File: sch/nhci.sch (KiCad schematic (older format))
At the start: 17 parts, among them IC1 74LVC8T245RHLRG4, IC2 74LVC8T245RHLRG4, IC3 74LVC8T245RHLRG4, IC4 74LVC8T245RHLRG4, IC5 74LVC8T245RHLRG4, SW1 SW_Push_Open, U1 PCMCIA_BOARD

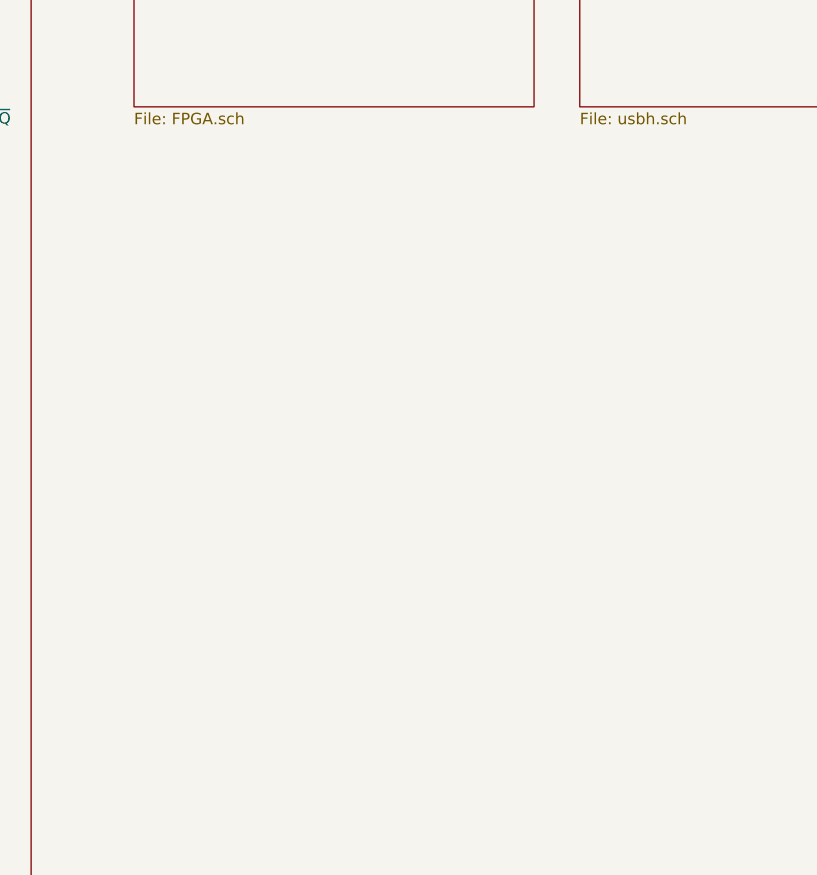
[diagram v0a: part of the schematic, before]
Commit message: Add pullup resistors
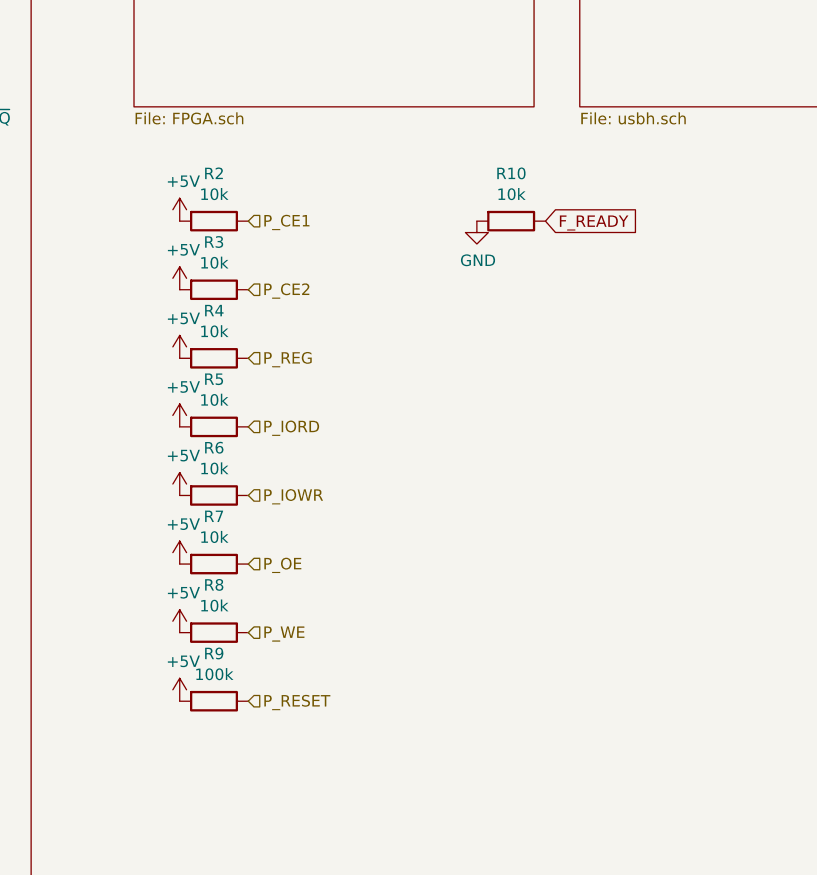
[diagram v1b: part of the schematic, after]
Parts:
- added R10, R2, R3, R4, R5, R6, R7, R8: 10k, Resistor_SMD:R_0402_1005Metric, symbol Device:R
- added R9: 100k, Resistor_SMD:R_0402_1005Metric, symbol Device:R
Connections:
- net +5V: now also R2.2, R3.2, R4.2, R5.2, R6.2, R7.2, R8.2, R9.2
- net F_READY: now also R10.1
- net GND: now also R10.2
- net P_CE1: now also R2.1
- net P_CE2: now also R3.1
- net P_IORD: now also R5.1
- net P_IOWR: now also R6.1
- net P_OE: now also R7.1
- net P_REG: now also R4.1
- net P_RESET: now also R9.1
- net P_WE: now also R8.1
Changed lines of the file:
@@
 F1 "usbh.sch" 50
 $EndSheet
+$Comp
+L Device:R R2
+U 1 1 60E72B90
+P 7550 4300
+F 0 "R2" V 7343 4300 50  0000 C CNN
+F 1 "10k" V 7434 4300 50  0000 C CNN
+F 2 "Resistor_SMD:R_0402_1005Metric" V 7480 4300 50  0001 C CNN
+F 3 "~" H 7550 4300 50  0001 C CNN
+	1    7550 4300
+	0    1    1    0
+$EndComp
+$Comp
+L power:+5V #PWR0168
+U 1 1 60E83325
+P 7400 4300
+F 0 "#PWR0168" H 7400 4150 50  0001 C CNN
+F 1 "+5V" H 7415 4473 50  0000 C CNN
+F 2 "" H 7400 4300 50  0001 C CNN
+F 3 "" H 7400 4300 50  0001 C CNN
+	1    7400 4300
+	1    0    0    -1
+$EndComp
+$Comp
+L Device:R R3
+U 1 1 60E86D97
+P 7550 4600
+F 0 "R3" V 7343 4600 50  0000 C CNN
+F 1 "10k" V 7434 4600 50  0000 C CNN
+F 2 "Resistor_SMD:R_0402_1005Metric" V 7480 4600 50  0001 C CNN
+F 3 "~" H 7550 4600 50  0001 C CNN
+	1    7550 4600
+	0    1    1    0
+$EndComp
+$Comp
+L power:+5V #PWR0169
+U 1 1 60E86D9D
+P 7400 4600
+F 0 "#PWR0169" H 7400 4450 50  0001 C CNN
+F 1 "+5V" H 7415 4773 50  0000 C CNN
+F 2 "" H 7400 4600 50  0001 C CNN
+F 3 "" H 7400 4600 50  0001 C CNN
+	1    7400 4600
+	1    0    0    -1
+$EndComp
+$Comp
+L Device:R R4
+U 1 1 60E877D1
+P 7550 4900
+F 0 "R4" V 7343 4900 50  0000 C CNN
+F 1 "10k" V 7434 4900 50  0000 C CNN
+F 2 "Resistor_SMD:R_0402_1005Metric" V 7480 4900 50  0001 C CNN
+F 3 "~" H 7550 4900 50  0001 C CNN
+	1    7550 4900
+	0    1    1    0
+$EndComp
+$Comp
+L power:+5V #PWR0170
+U 1 1 60E877D7
+P 7400 4900
+F 0 "#PWR0170" H 7400 4750 50  0001 C CNN
+F 1 "+5V" H 7415 5073 50  0000 C CNN
+F 2 "" H 7400 4900 50  0001 C CNN
+F 3 "" H 7400 4900 50  0001 C CNN
+	1    7400 4900
+	1    0    0    -1
+$EndComp
+$Comp
+L Device:R R5
+U 1 1 60E88331
+P 7550 5200
+F 0 "R5" V 7343 5200 50  0000 C CNN
+F 1 "10k" V 7434 5200 50  0000 C CNN
+F 2 "Resistor_SMD:R_0402_1005Metric" V 7480 5200 50  0001 C CNN
+F 3 "~" H 7550 5200 50  0001 C CNN
+	1    7550 5200
+	0    1    1    0
+$EndComp
+$Comp
+L power:+5V #PWR0171
+U 1 1 60E88337
+P 7400 5200
+F 0 "#PWR0171" H 7400 5050 50  0001 C CNN
+F 1 "+5V" H 7415 5373 50  0000 C CNN
+F 2 "" H 7400 5200 50  0001 C CNN
+F 3 "" H 7400 5200 50  0001 C CNN
+	1    7400 5200
+	1    0    0    -1
+$EndComp
+$Comp
+L Device:R R6
+U 1 1 60E88E3B
+P 7550 5500
+F 0 "R6" V 7343 5500 50  0000 C CNN
+F 1 "10k" V 7434 5500 50  0000 C CNN
+F 2 "Resistor_SMD:R_0402_1005Metric" V 7480 5500 50  0001 C CNN
+F 3 "~" H 7550 5500 50  0001 C CNN
+	1    7550 5500
+	0    1    1    0
+$EndComp
+$Comp
+L power:+5V #PWR0172
+U 1 1 60E88E41
+P 7400 5500
+F 0 "#PWR0172" H 7400 5350 50  0001 C CNN
+F 1 "+5V" H 7415 5673 50  0000 C CNN
+F 2 "" H 7400 5500 50  0001 C CNN
+F 3 "" H 7400 5500 50  0001 C CNN
+	1    7400 5500
+	1    0    0    -1
+$EndComp
+$Comp
+L Device:R R7
+U 1 1 60E8A04D
+P 7550 5800
+F 0 "R7" V 7343 5800 50  0000 C CNN
+F 1 "10k" V 7434 5800 50  0000 C CNN
+F 2 "Resistor_SMD:R_0402_1005Metric" V 7480 5800 50  0001 C CNN
+F 3 "~" H 7550 5800 50  0001 C CNN
+	1    7550 5800
+	0    1    1    0
+$EndComp
+$Comp
+L power:+5V #PWR0173
+U 1 1 60E8A053
+P 7400 5800
+F 0 "#PWR0173" H 7400 5650 50  0001 C CNN
+F 1 "+5V" H 7415 5973 50  0000 C CNN
+F 2 "" H 7400 5800 50  0001 C CNN
+F 3 "" H 7400 5800 50  0001 C CNN
+	1    7400 5800
+	1    0    0    -1
+$EndComp
+$Comp
+L Device:R R8
+U 1 1 60E8AC09
+P 7550 6100
+F 0 "R8" V 7343 6100 50  0000 C CNN
+F 1 "10k" V 7434 6100 50  0000 C CNN
+F 2 "Resistor_SMD:R_0402_1005Metric" V 7480 6100 50  0001 C CNN
+F 3 "~" H 7550 6100 50  0001 C CNN
+	1    7550 6100
+	0    1    1    0
+$EndComp
+$Comp
+L power:+5V #PWR0174
+U 1 1 60E8AC0F
+P 7400 6100
+F 0 "#PWR0174" H 7400 5950 50  0001 C CNN
+F 1 "+5V" H 7415 6273 50  0000 C CNN
+F 2 "" H 7400 6100 50  0001 C CNN
+F 3 "" H 7400 6100 50  0001 C CNN
+	1    7400 6100
+	1    0    0    -1
+$EndComp
+$Comp
+L Device:R R9
+U 1 1 60E8BA17
+P 7550 6400
+F 0 "R9" V 7343 6400 50  0000 C CNN
+F 1 "100k" V 7434 6400 50  0000 C CNN
+F 2 "Resistor_SMD:R_0402_1005Metric" V 7480 6400 50  0001 C CNN
+F 3 "~" H 7550 6400 50  0001 C CNN
+	1    7550 6400
+	0    1    1    0
+$EndComp
+$Comp
+L power:+5V #PWR0175
+U 1 1 60E8BA1D
+P 7400 6400
+F 0 "#PWR0175" H 7400 6250 50  0001 C CNN
+F 1 "+5V" H 7415 6573 50  0000 C CNN
+F 2 "" H 7400 6400 50  0001 C CNN
+F 3 "" H 7400 6400 50  0001 C CNN
+	1    7400 6400
+	1    0    0    -1
+$EndComp
+Text HLabel 7700 4300 2    50   Input ~ 0
+P_CE1
+Text HLabel 7700 4600 2    50   Input ~ 0
+P_CE2
+Text HLabel 7700 4900 2    50   Input ~ 0
+P_REG
+Text HLabel 7700 5200 2    50   Input ~ 0
+P_IORD
+Text HLabel 7700 5500 2    50   Input ~ 0
+P_IOWR
+Text HLabel 7700 5800 2    50   Input ~ 0
+P_OE
+Text HLabel 7700 6100 2    50   Input ~ 0
+P_WE
+Text HLabel 7700 6400 2    50   Input ~ 0
+P_RESET
+$Comp
+L Device:R R10
+U 1 1 60E92A91
+P 8850 4300
+F 0 "R10" V 8643 4300 50  0000 C CNN
+F 1 "10k" V 8734 4300 50  0000 C CNN
+F 2 "Resistor_SMD:R_0402_1005Metric" V 8780 4300 50  0001 C CNN
+F 3 "~" H 8850 4300 50  0001 C CNN
+	1    8850 4300
+	0    1    1    0
+$EndComp
+$Comp
+L power:GND #PWR0176
+U 1 1 60E95B19
+P 8700 4300
+F 0 "#PWR0176" H 8700 4050 50  0001 C CNN
+F 1 "GND" H 8705 4127 50  0000 C CNN
+F 2 "" H 8700 4300 50  0001 C CNN
+F 3 "" H 8700 4300 50  0001 C CNN
+	1    8700 4300
+	1    0    0    -1
+$EndComp
+Text GLabel 9000 4300 2    50   Input ~ 0
+F_READY
 $EndSCHEMATC

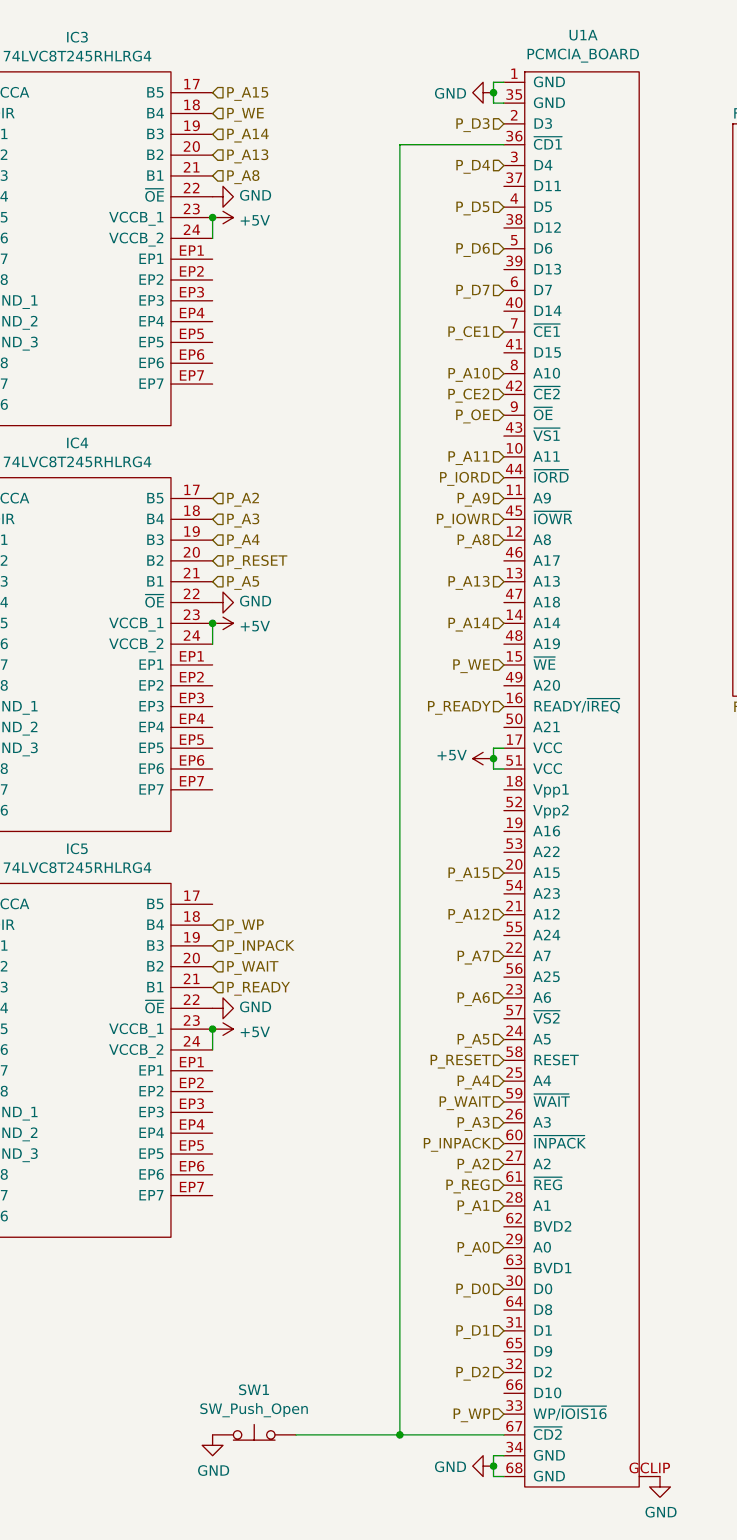
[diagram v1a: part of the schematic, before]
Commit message: Add solder jumper for non development board
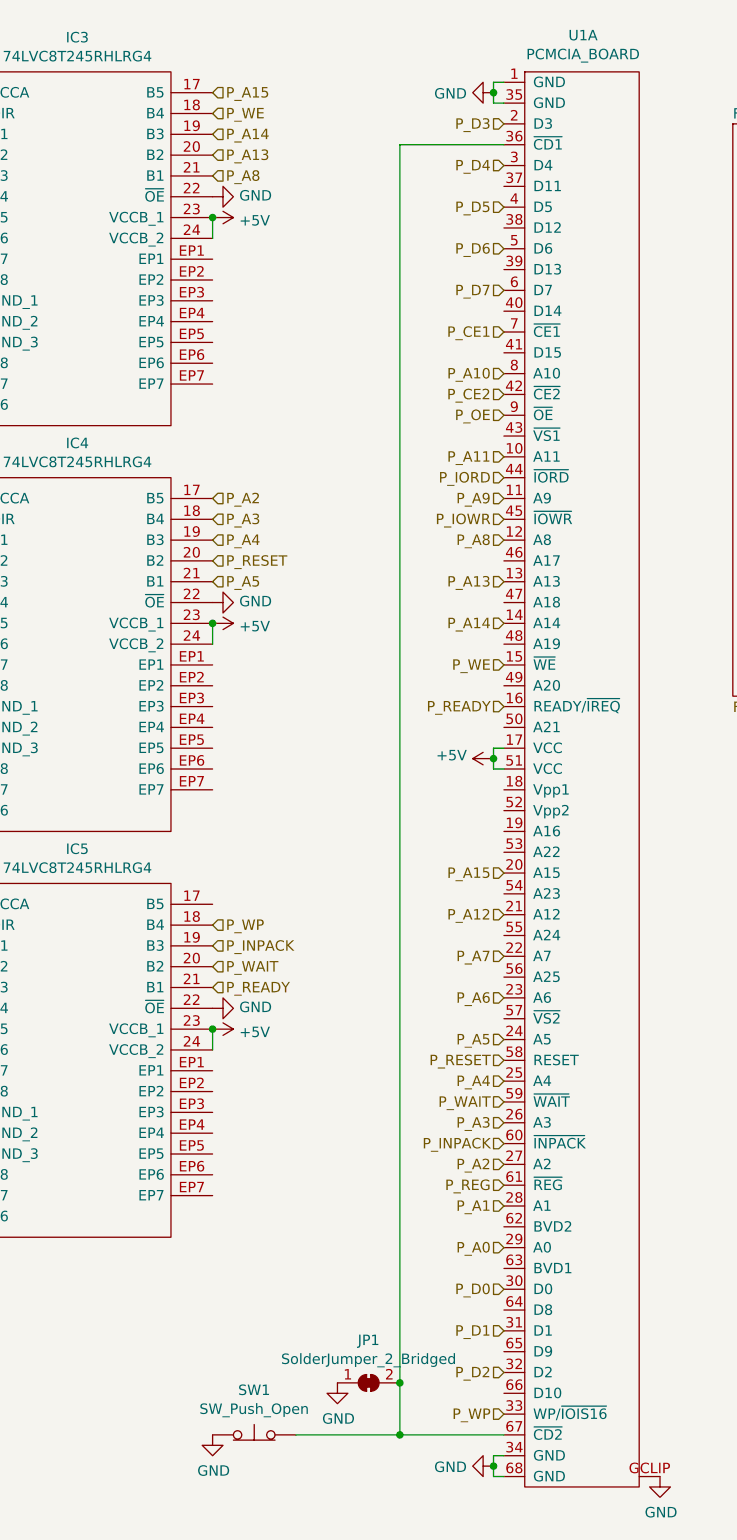
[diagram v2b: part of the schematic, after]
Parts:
- added JP1: SolderJumper_2_Bridged, Jumper:SolderJumper-2_P1.3mm_Bridged2Bar_RoundedPad1.0x1.5mm, symbol Jumper:SolderJumper_2_Bridged
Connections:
- net GND: now also JP1.1 (A)
- net at SW1.2 (B), U1.36 (~CD1), U1.67 (~CD2): now also JP1.2 (B)
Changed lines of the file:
@@
 	6100 1150 5600 1150
 Wire Wire Line
-	5600 1150 5600 7350
+	5600 1150 5600 7100
 Connection ~ 5600 7350
 Wire Wire Line
@@
 Text GLabel 9000 4300 2    50   Input ~ 0
 F_READY
+$Comp
+L Jumper:SolderJumper_2_Bridged JP1
+U 1 1 60FACB1B
+P 5450 7100
+F 0 "JP1" H 5450 7305 50  0000 C CNN
+F 1 "SolderJumper_2_Bridged" H 5450 7214 50  0000 C CNN
+F 2 "Jumper:SolderJumper-2_P1.3mm_Bridged2Bar_RoundedPad1.0x1.5mm" H 5450 7100 50  0001 C CNN
+F 3 "~" H 5450 7100 50  0001 C CNN
+	1    5450 7100
+	1    0    0    -1
+$EndComp
+Connection ~ 5600 7100
+Wire Wire Line
+	5600 7100 5600 7350
+$Comp
+L power:GND #PWR0194
+U 1 1 60FAD98F
+P 5300 7100
+F 0 "#PWR0194" H 5300 6850 50  0001 C CNN
+F 1 "GND" H 5305 6927 50  0000 C CNN
+F 2 "" H 5300 7100 50  0001 C CNN
+F 3 "" H 5300 7100 50  0001 C CNN
+	1    5300 7100
+	1    0    0    -1
+$EndComp
 $EndSCHEMATC
